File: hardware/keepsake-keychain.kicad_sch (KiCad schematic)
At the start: 5 parts, among them SW1 SPDT Power Switch, U1 74HC595, U2 ATTINY1614-SSF

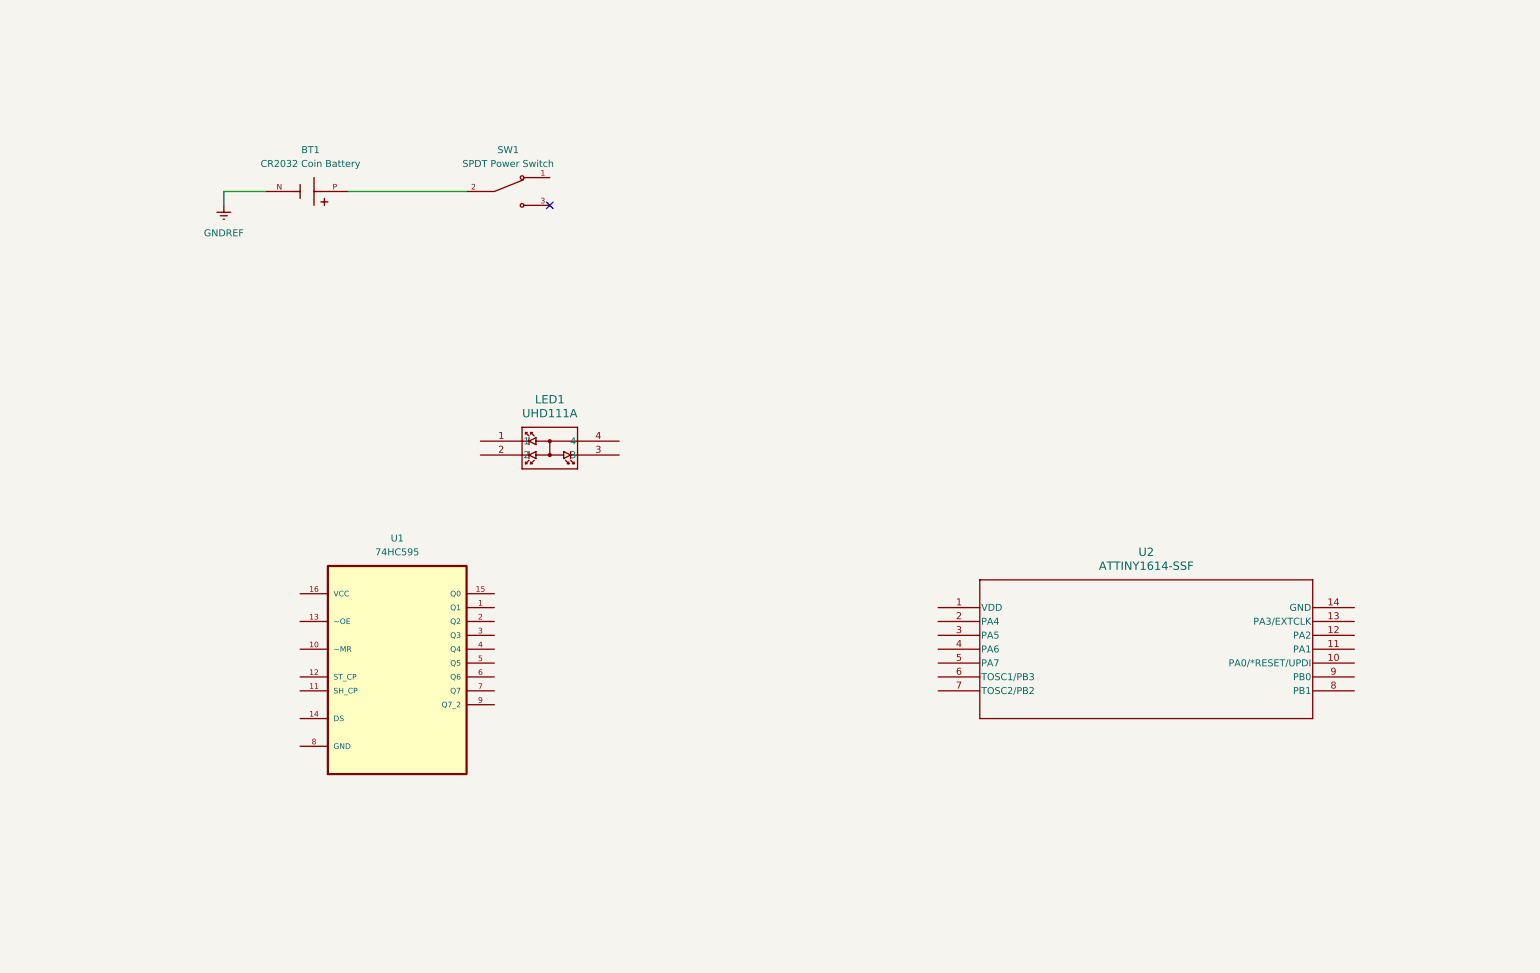
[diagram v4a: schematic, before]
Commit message: Add P-channel MOSFET
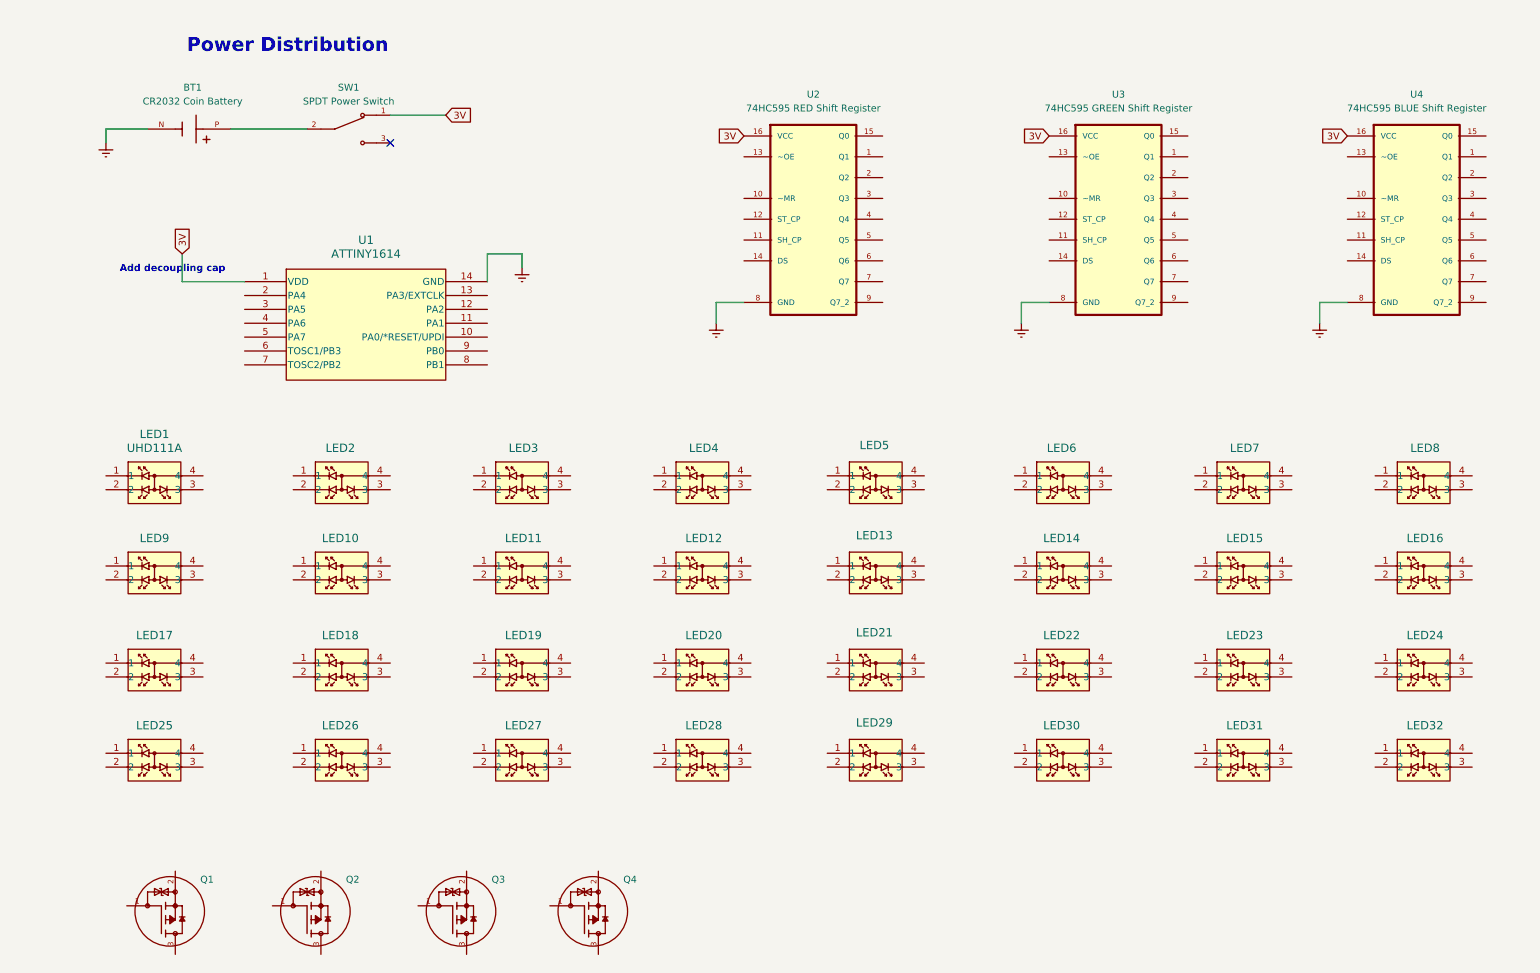
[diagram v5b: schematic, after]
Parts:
- added LED10, LED11, LED12, LED13, LED14, LED15, LED16, LED17, LED18, LED19, LED2, LED20, LED21, LED22, LED23, LED24, LED25, LED26, LED27, LED28, LED29, LED3, LED30, LED31, LED32, LED4, LED5, LED6, LED7, LED8, LED9: UHD111A, 0_RGB_LED:rgb-led, symbol 0_RGB_LED:UHD111A-FKA-C3K23E1L3VG5ZB3Z3
- added Q1, Q2, Q3, Q4: MMFTP4042K, 0_MOSFET:mosfet, symbol 0_MOSFET:MMFTP4042K
- added U3: 74HC595 GREEN Shift Register, 0_74HC595_Shift_Register:shift-register, symbol 0_74HC595_Shift_Register:74HC595PW_118
- added U4: 74HC595 BLUE Shift Register, 0_74HC595_Shift_Register:shift-register, symbol 0_74HC595_Shift_Register:74HC595PW_118
- BT1: footprint BH-25C-1:BAT_BH-25C-1 -> digikey-footprints:Battery_Holder_Coin_2032_BS-7; symbol 0_Button_Cell_Holder:BH-25C-1 -> 0_Coin_Battery_Holder:BH-25C-1
- LED1: footprint SMD4_UHD111A-FKA_CRW -> 0_RGB_LED:rgb-led
- SW1: footprint SLW-129956-4A-RA-N-D:SW_SLW-129956-4A-RA-N-D -> 0_SPDT_Switch:spdt-switch
- U1: renamed from U2; value ATTINY1614-SSF -> ATTINY1614; footprint SOIC14_SL_MCH -> 0_ATtiny1614:SOIC14_SL_MCH-M
- U2: renamed from U1; value 74HC595 -> 74HC595 RED Shift Register; footprint 74HC595PW_118:SOP65P640X110-16N -> 0_74HC595_Shift_Register:shift-register
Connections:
- net GNDREF is gone; now on net GND: BT1.N
- net 3V: now reaches U1.1 (VDD)
- net 3V: now also SW1.1, U2.16 (VCC), U3.16 (VCC), U4.16 (VCC)
- net GND: now reaches U1.14 (GND)
- net GND: now also U2.8 (GND), U3.8 (GND), U4.8 (GND)
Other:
- note added: "Add decoupling cap"
- note added: "Power Distribution"
- moved on the sheet: BT1, SW1, U2

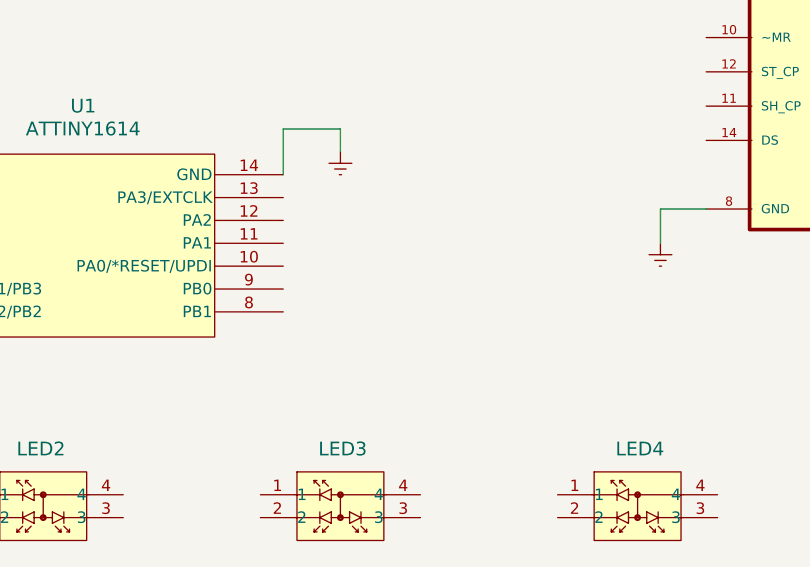
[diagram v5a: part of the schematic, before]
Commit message: Add pin for UPDI programming
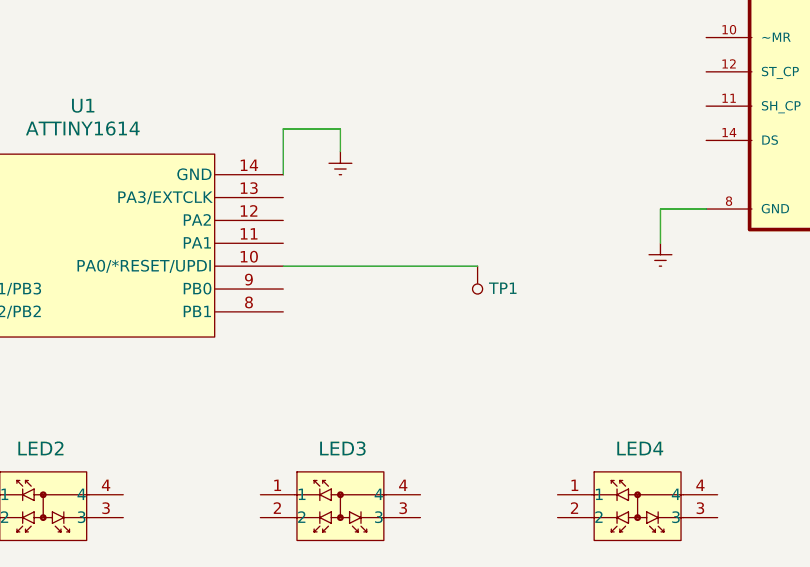
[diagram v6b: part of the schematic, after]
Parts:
- added TP1: 5002, digikey-footprints:Test_Point_D1.02mm, symbol dk_Test-Points:5002
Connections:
- net at U1.10 (PA0/*RESET/UPDI): now also TP1.1
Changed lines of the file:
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@@
 	(wire
 		(pts
+			(xy 93.98 77.47) (xy 115.57 77.47)
+		)
+		(stroke
+			(width 0)
+			(type default)
+		)
+	)
+	(wire
+		(pts
 			(xy 196.85 71.12) (xy 191.77 71.12)
 		)
@@
 					(unit 1)
 				)
+			)
+		)
+	)
+	(symbol
+		(lib_id "dk_Test-Points:5002")
+		(at 115.57 80.01 0)
+		(unit 1)
+		(exclude_from_sim no)
+		(in_bom yes)
+		(on_board yes)
+		(dnp no)
+		(fields_autoplaced yes)
+		(property "Reference" "TP1"
+			(at 116.84 79.9718 0)
+			(effects
+				(font
+					(size 1.27 1.27)
+				)
+				(justify left)
+			)
+		)
+		(property "Value" "5002"
+			(at 115.57 82.55 0)
+			(effects
+				(font
+					(size 1.27 1.27)
+				)
+				(hide yes)
+			)
+		)
+		(property "Footprint" "digikey-footprints:Test_Point_D1.02mm"
+			(at 120.65 74.93 0)
+			(effects
+				(font
+					(size 1.524 1.524)
+				)
+				(justify left)
+				(hide yes)
+			)
+		)
+		(property "Datasheet" "http://www.keyelco.com/product-pdf.cfm?p=1311"
+			(at 120.65 72.39 0)
+			(effects
+				(font
+					(size 1.524 1.524)
+				)
+				(justify left)
+				(hide yes)
+			)
+		)
+		(property "Description" "PC TEST POINT MINIATURE WHITE"
+			(at 115.57 80.01 0)
+			(effects
+				(font
+					(size 1.27 1.27)
+				)
+				(hide yes)
+			)
+		)
+		(property "Digi-Key_PN" "36-5002-ND"
+			(at 120.65 69.85 0)
+			(effects
+				(font
+					(size 1.524 1.524)
+				)
+				(justify left)
+				(hide yes)
+			)
+		)
+		(property "MPN" "5002"
+			(at 120.65 67.31 0)
+			(effects
+				(font
+					(size 1.524 1.524)
+				)
+				(justify left)
+				(hide yes)
+			)
+		)
+		(property "Category" "Test and Measurement"
+			(at 120.65 64.77 0)
+			(effects
+				(font
+					(size 1.524 1.524)
+				)
+				(justify left)
+				(hide yes)
+			)
+		)
+		(property "Family" "Test Points"
+			(at 120.65 62.23 0)
+			(effects
+				(font
+					(size 1.524 1.524)
+				)
+				(justify left)
+				(hide yes)
+			)
+		)
+		(property "DK_Datasheet_Link" "http://www.keyelco.com/product-pdf.cfm?p=1311"
+			(at 120.65 59.69 0)
+			(effects
+				(font
+					(size 1.524 1.524)
+				)
+				(justify left)
+				(hide yes)
+			)
+		)
+		(property "DK_Detail_Page" "/product-detail/en/keystone-electronics/5002/36-5002-ND/255328"
+			(at 120.65 57.15 0)
+			(effects
+				(font
+					(size 1.524 1.524)
+				)
+				(justify left)
+				(hide yes)
+			)
+		)
+		(property "Description_1" "PC TEST POINT MINIATURE WHITE"
+			(at 120.65 54.61 0)
+			(effects
+				(font
+					(size 1.524 1.524)
+				)
+				(justify left)
+				(hide yes)
+			)
+		)
+		(property "Manufacturer" "Keystone Electronics"
+			(at 120.65 52.07 0)
+			(effects
+				(font
+					(size 1.524 1.524)
+				)
+				(justify left)
+				(hide yes)
+			)
+		)
+		(property "Status" "Active"
+			(at 120.65 49.53 0)
+			(effects
+				(font
+					(size 1.524 1.524)
+				)
+				(justify left)
+				(hide yes)
+			)
+		)
+		(pin "1"
+		)
+		(instances
+			(project ""
+				(path "/32670795-e352-430d-9b7f-c7f10ebe6399"
+					(reference "TP1")
+					(unit 1)
+				)

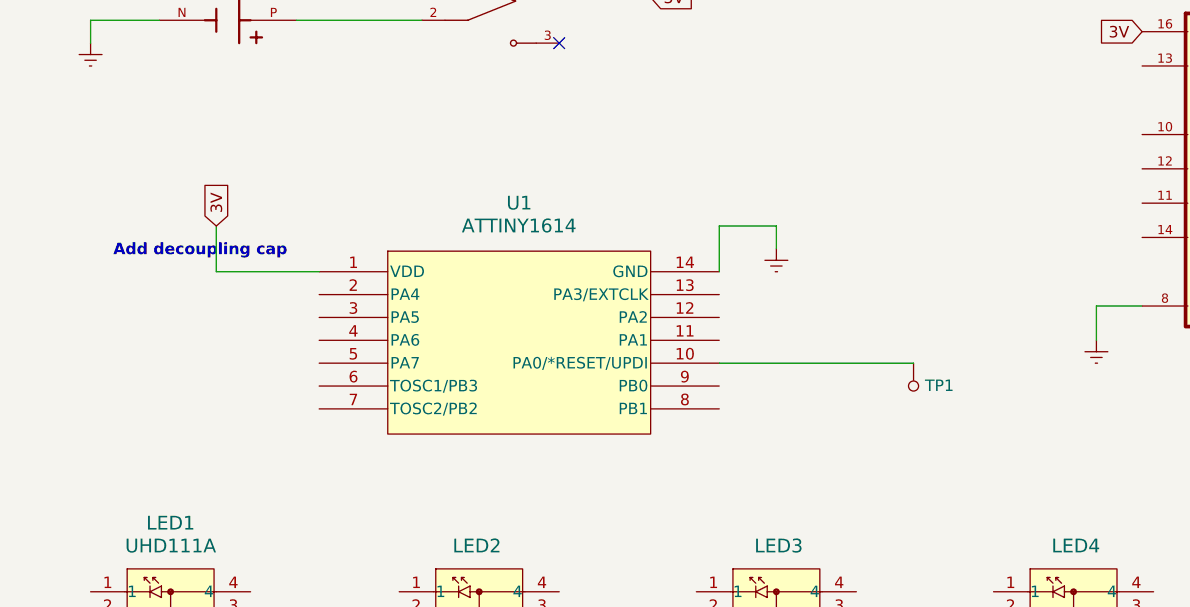
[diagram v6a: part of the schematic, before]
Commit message: Add tactile push button
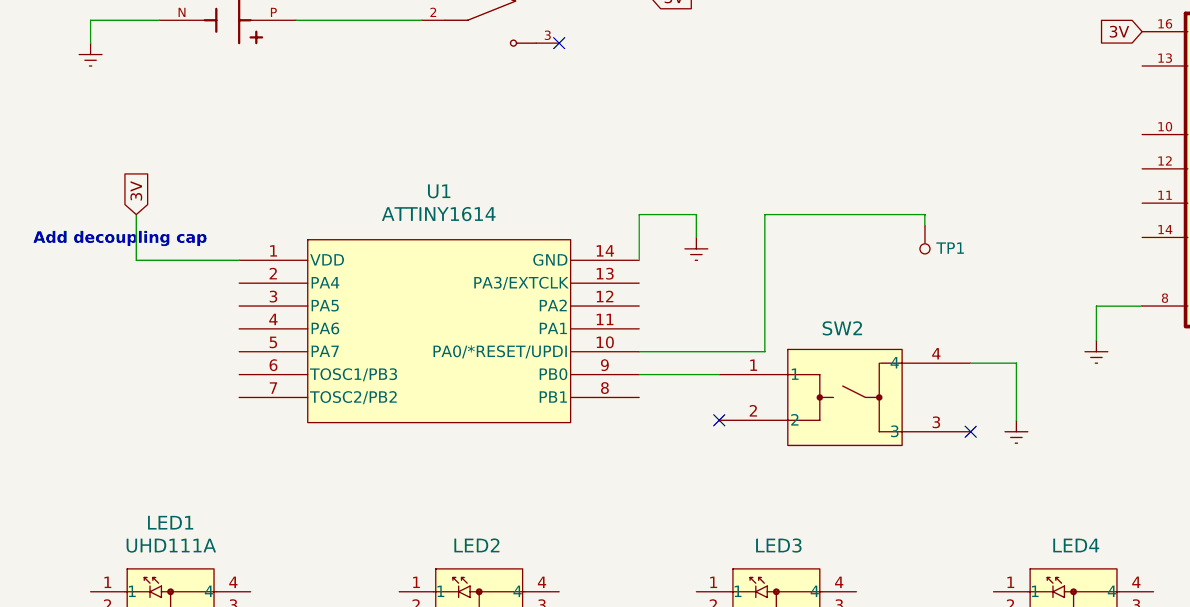
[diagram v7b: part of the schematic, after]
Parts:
- added SW2: R-667842, R-667_MIT, symbol 0_Tactile_Push_Button:R-667842
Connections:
- net GND: now also SW2.4
- net at U1.9 (PB0): now also SW2.1
- no-connect marks 1 -> 3
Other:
- moved on the sheet: TP1, U1
